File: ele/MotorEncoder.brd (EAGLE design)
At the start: 15 x 16 mm, 13 parts, among them X1 PHB_1MM27_2X03_SNT_S, X2 PHB_1MM27_2X03_SNT_S

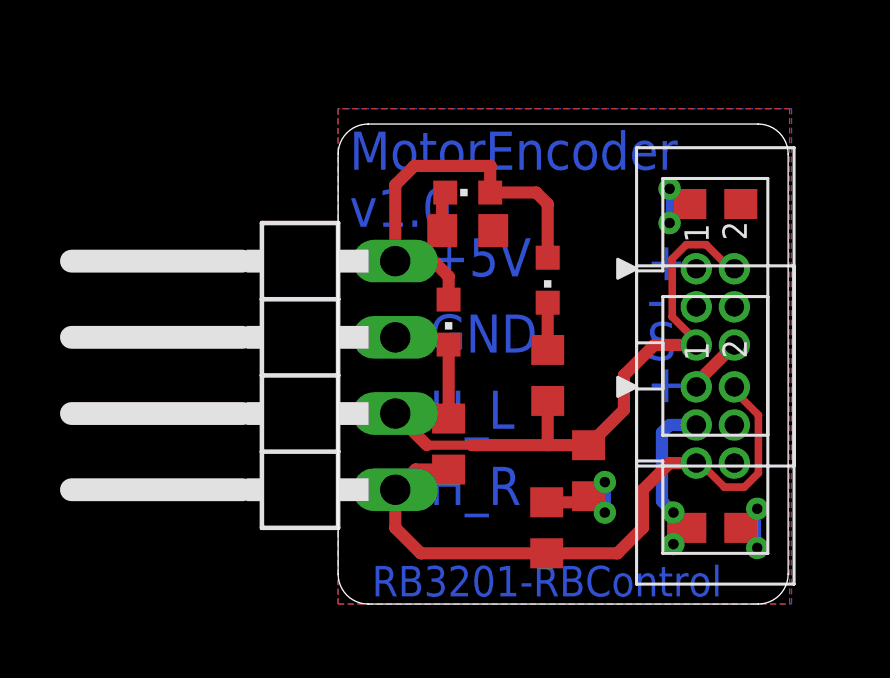
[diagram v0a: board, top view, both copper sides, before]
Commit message: ele: Reroute MotorEncoder
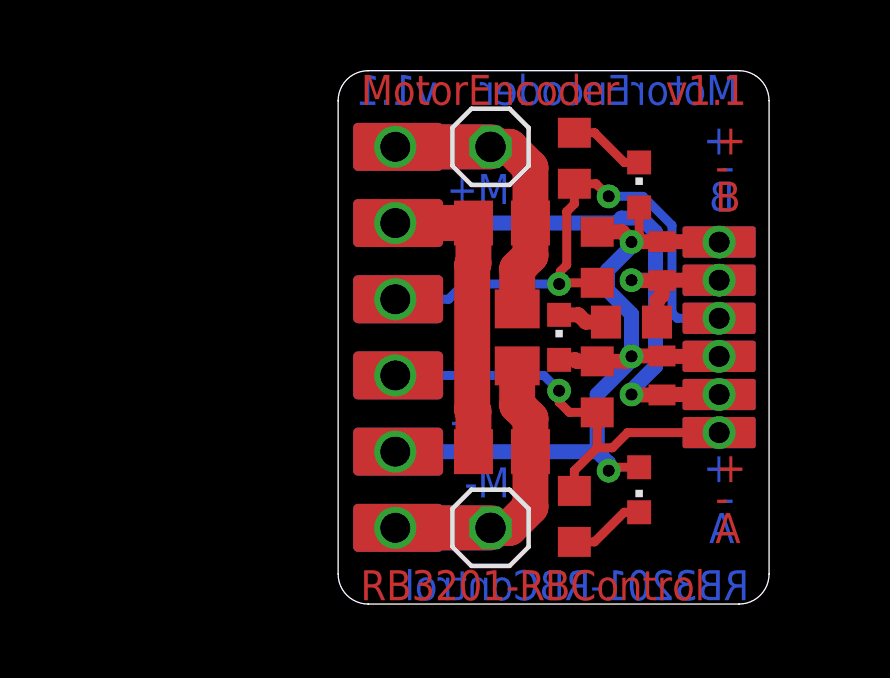
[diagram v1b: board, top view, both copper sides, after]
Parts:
- removed JP3: CON, pinhead:1X04/90
- removed X1, X2: PHB_1MM27_2X03_SNT_S, _hhn_con_pinhead_box_1mm27:PHB_1MM27_2X03_SNT
- added C3, C4, C5: 330n/50V, rcl:C0805
- added HS1, HS2: (no value), HallSensor:SMD/TH
- added JP1: PINH2X06, pinhead_smd:PINH2X06SMD
- added JP2, JP4: (no value), pinhead:1X01
- C1: value 100n/6,3V -> 100n/6.3V; device rcl:C0603 -> rcl:C0402
- C2: value 100n/6,3V, -> 100n/6.3V; device rcl:C0603 -> rcl:C0402
- moved R5 10.4 mm to (7.87, 14.9)
- moved R3 9.17 mm to (8.64, 11.6)
- moved C2 9.07 mm to (10.8, 11.4), turned to 270 degrees
- moved LED_SIDE1 7.82 mm to (10.0, 14.0), turned to 0 degrees
- moved LED_TOP1 7.62 mm to (10.0, 3.81)
- moved R1 6.25 mm to (9.78, 9.40)
- moved C1 5.99 mm to (10.8, 7.62), turned to 270 degrees
- moved LED_POWER 5.71 mm to (7.37, 8.89), turned to 0 degrees
- moved R4 4.78 mm to (7.87, 2.92), turned to 270 degrees
- moved R2 2.81 mm to (8.64, 7.24), turned to 90 degrees
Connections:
- removed net HAL_LEFT: JP3.2, R2.1, R4.1, X1.2, X1.5
- removed net HAL_RIGHT: JP3.1, R3.1, R5.1, X2.2, X2.5
- new net A: HS1.OUT, JP1.B3, JP1.T3, R2.1, R4.1
- new net B: HS2.OUT, JP1.B4, JP1.T4, R3.1, R5.1
- new net M+: C3.1, C5.1, JP1.B6, JP1.T6, JP4.1
- new net M-: C4.1, C5.2, JP1.B1, JP1.T1, JP2.1
- net +5V: now also HS1.VCC, HS2.VCC, JP1.B2, JP1.T2; no longer JP3.4, X1.1, X1.6, X2.1, X2.6
- net GND: now also C3.2, C4.2, HS1.GND, HS2.GND, JP1.B5, JP1.T5; no longer JP3.3, X1.3, X1.4, X2.3, X2.4
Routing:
- net GND: track 6.17 -> 33.2 mm, vias 2 -> 3
- net HAL_LEFT: track 23.7 -> 0.00 mm
- net HAL_RIGHT: track 21.6 -> 0.00 mm
- net B: track 0.00 -> 19.0 mm, vias 0 -> 3
- net A: track 0.00 -> 14.8 mm, vias 0 -> 2
- net M-: track 0.00 -> 12.8 mm, vias 0 -> 1
- net M+: track 0.00 -> 12.8 mm, vias 0 -> 1
- net +5V: track 25.5 -> 27.9 mm, vias 6 -> 4
- net LED_TOP1: track 1.57 -> 2.57 mm
- removed copper zone on layer 16, net +5V
- removed copper zone on layer 1, net GND
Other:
- board size 15 x 16 mm -> 14.4 x 17.8 mm
- board text added: "A"
- board text added: "B"
- board text added: "M+"
- board text added: "M-"
- board text added: "v1.1"
- board text removed: "+5V"
- board text removed: "10k"
- board text removed: "GND"
- board text removed: "H_L"
- board text removed: "H_R"
- board text removed: "L:"
- board text removed: "MotorEncoder v1.0"
- board text removed: "ON"
- board text removed: "R:"
- board text removed: "S"
- board text removed: "v1.0"
